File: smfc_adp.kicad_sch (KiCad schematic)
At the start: 29 parts, among them J1 Conn_01x03_Pin, J11 Conn_01x02_Socket, J2 Conn_01x03_Pin, J25 Conn_01x02_Socket, J26 Conn_01x02_Socket, J4 Conn_01x04_Socket, U1 ADP5091

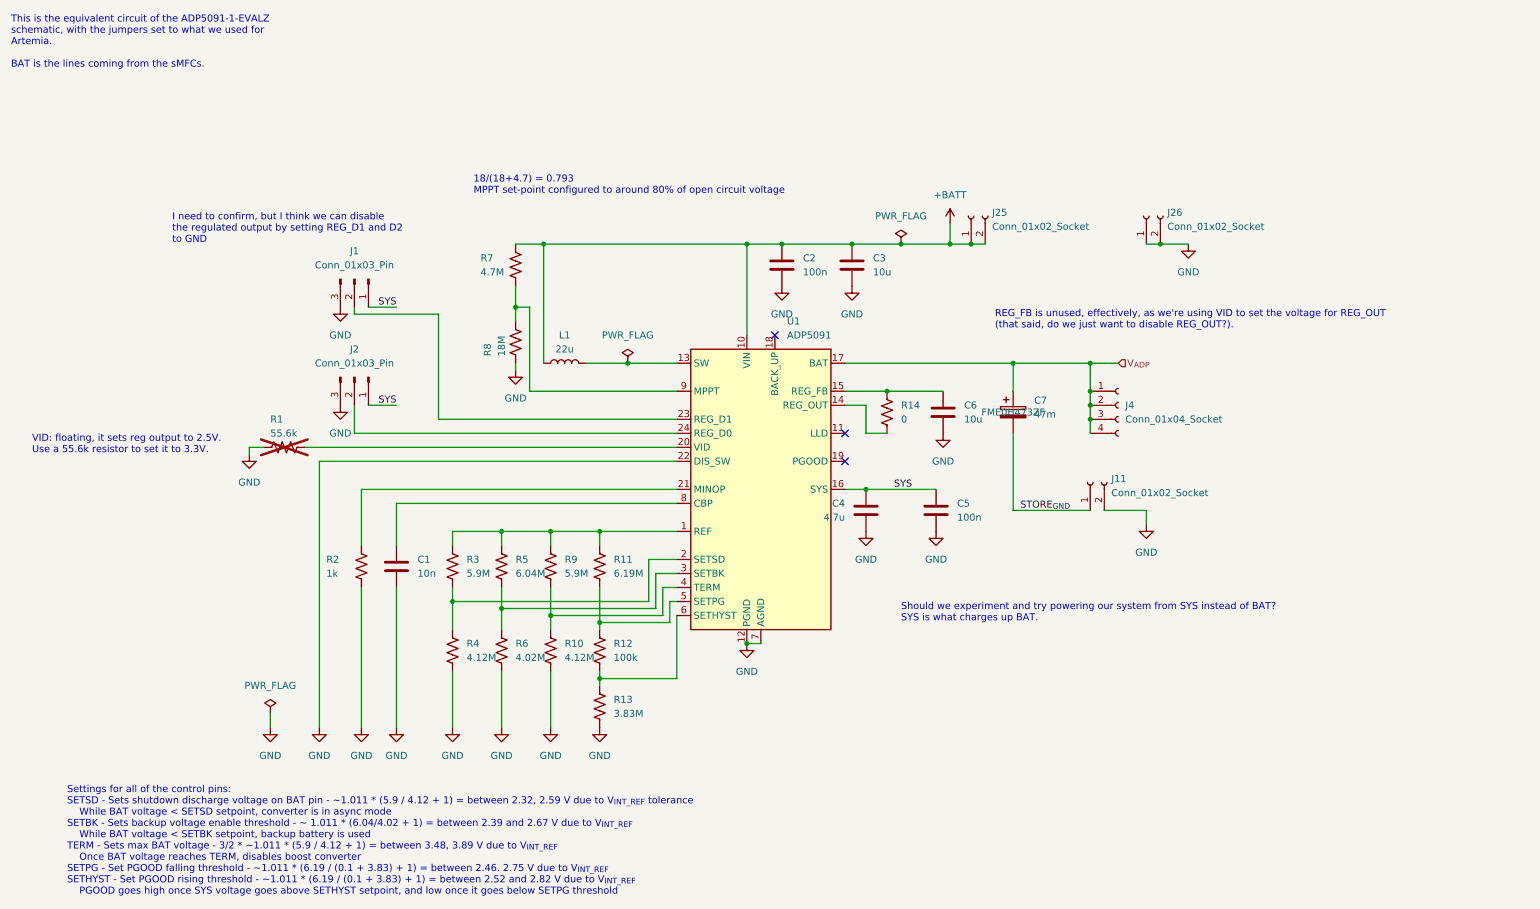
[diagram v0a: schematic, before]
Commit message: Add more informative text, crystal to SMD, headers
 - Added a lot more to the silkscreen to segment parts of the board
 - Changed the 32kHz crystals to an SMD part
 - Added some headers for ADP5091 function
 - Some BOM consolidation, mostly of resistors and capacitors
 - Marked one capacitor as C0G rating
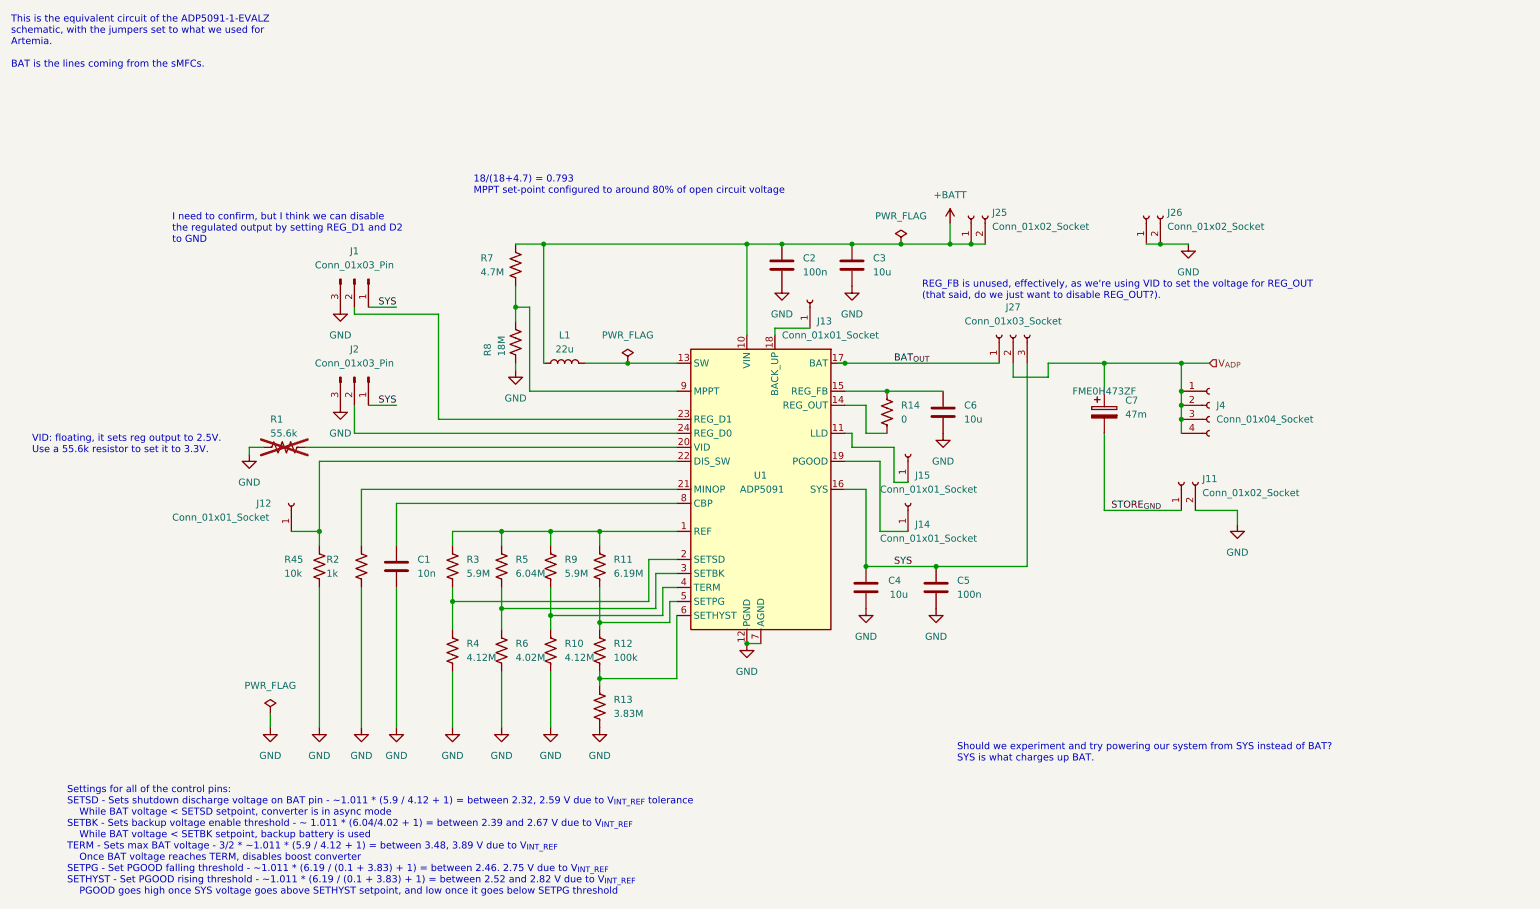
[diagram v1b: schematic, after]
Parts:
- added J12, J13, J14, J15: Conn_01x01_Socket, Connector_PinHeader_2.54mm:PinHeader_1x01_P2.54mm_Vertical, symbol Connector:Conn_01x01_Socket
- added J27: Conn_01x03_Socket, Connector_PinHeader_2.54mm:PinHeader_1x03_P2.54mm_Vertical, symbol Connector:Conn_01x03_Socket
- added R45: 10k, Resistor_SMD:R_0603_1608Metric_Pad0.98x0.95mm_HandSolder, symbol Device:R_US
- C1: Digikey Product Number (none) -> 490-GRT1885C1E103JA02JTR-ND; Manufacturer Product Number (none) -> GRT1885C1E103JA02J
- C4: value 4.7u -> 10u
- C7: Digikey Product Number (none) -> 399-13100-ND
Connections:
- net GND: now also R45.1; no longer U1.22 (DIS_SW)
- net SYS: now also J27.3 (Pin_3)
- net V_{ADP}: now also J27.2 (Pin_2); no longer U1.17 (BAT)
- net at U1.11 (LLD): now also J15.1 (Pin_1)
- net at U1.18 (BACK_UP): now also J13.1 (Pin_1)
- net at U1.19 (PGOOD): now also J14.1 (Pin_1)
- new net: J12.1 (Pin_1), R45.2, U1.22 (DIS_SW)
- new net BAT_{OUT}: J27.1 (Pin_1), U1.17 (BAT)
- no-connect marks 3 -> 0
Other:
- moved on the sheet: C4, C5, C7, J11, J4

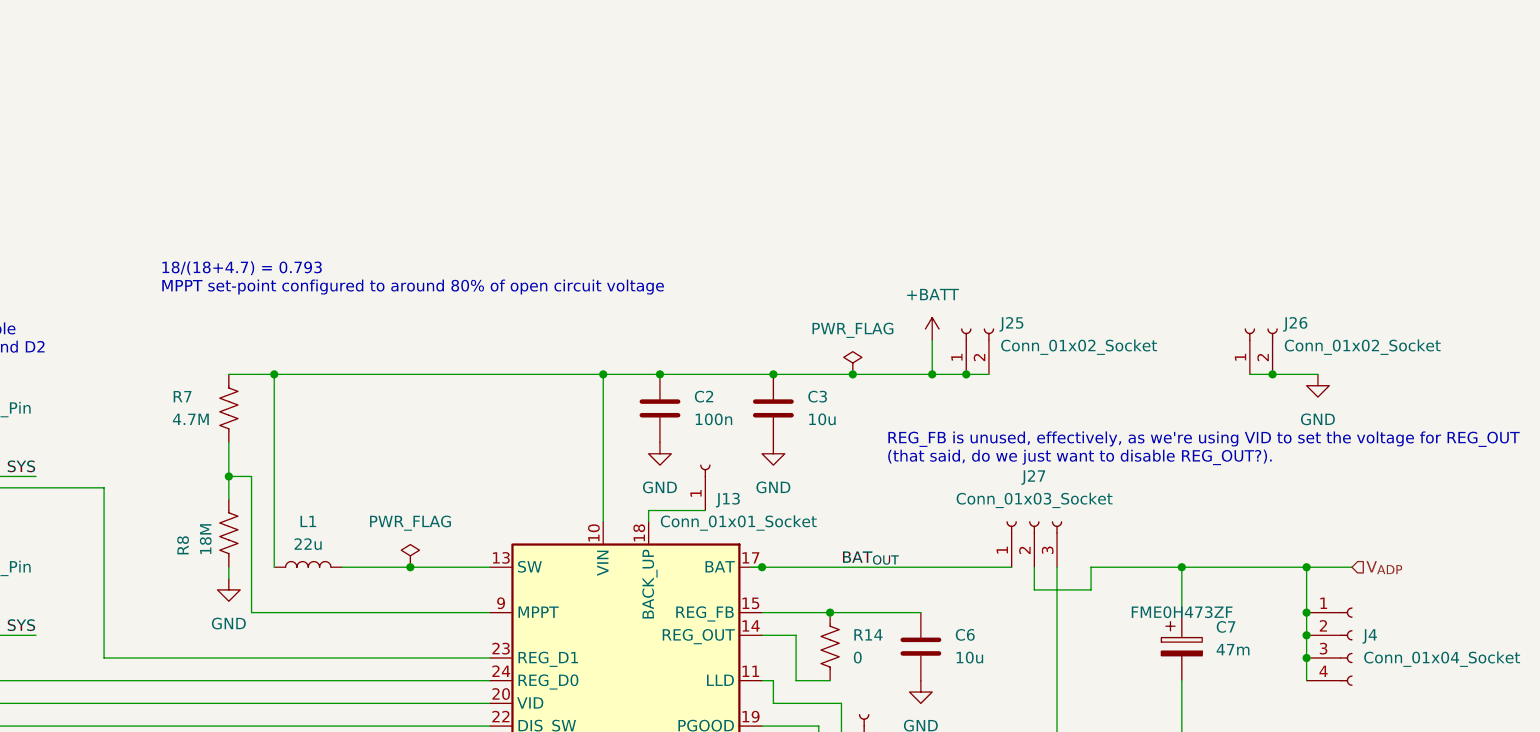
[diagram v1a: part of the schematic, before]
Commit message: Fix ERC, add MPN and datasheet information
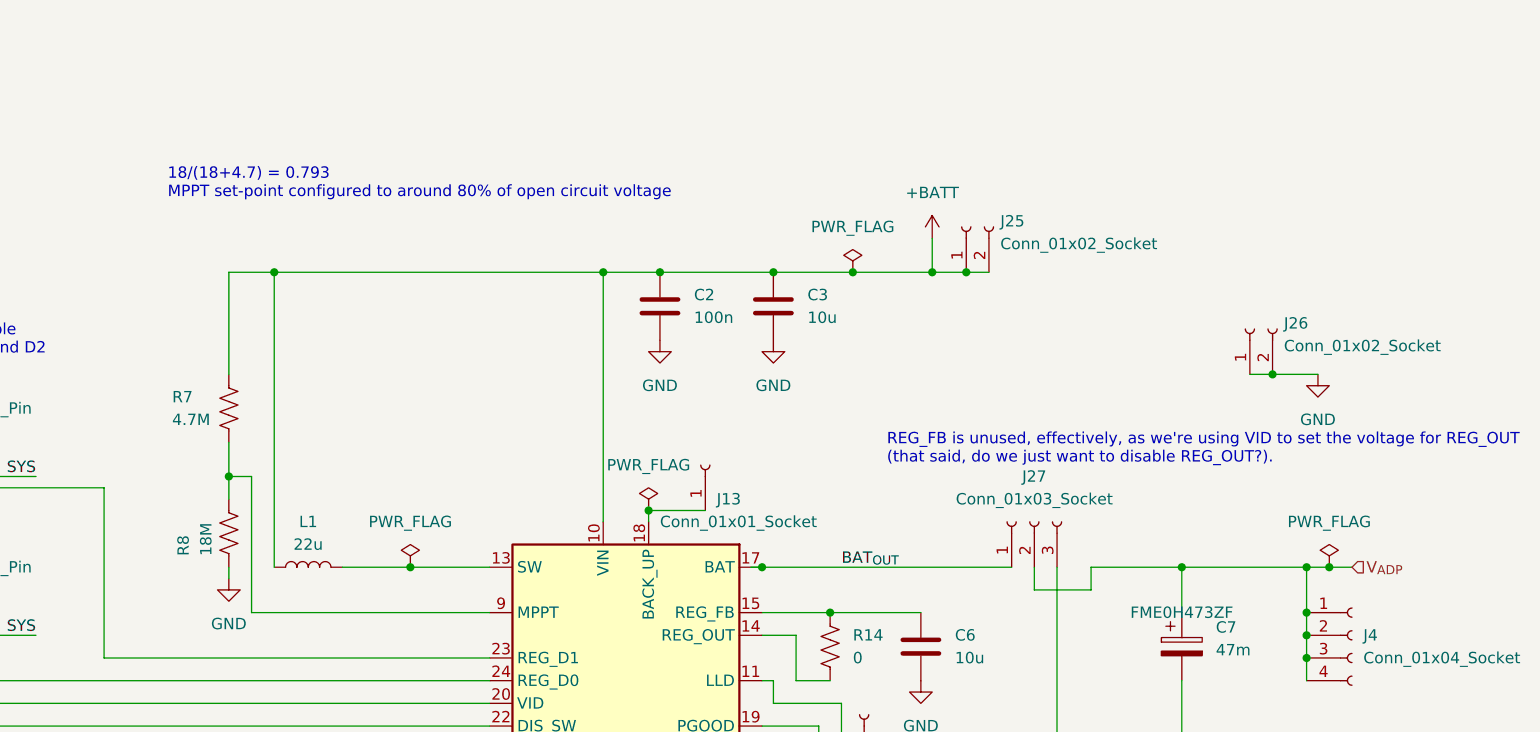
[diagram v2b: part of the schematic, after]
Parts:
- U1: Digikey Product Number (none) -> 505-ADP5091ACPZ-1-R7TR-ND; Manufacturer Product Number (none) -> ADP5091ACPZ-1-R7
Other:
- moved on the sheet: C2, C3, J25

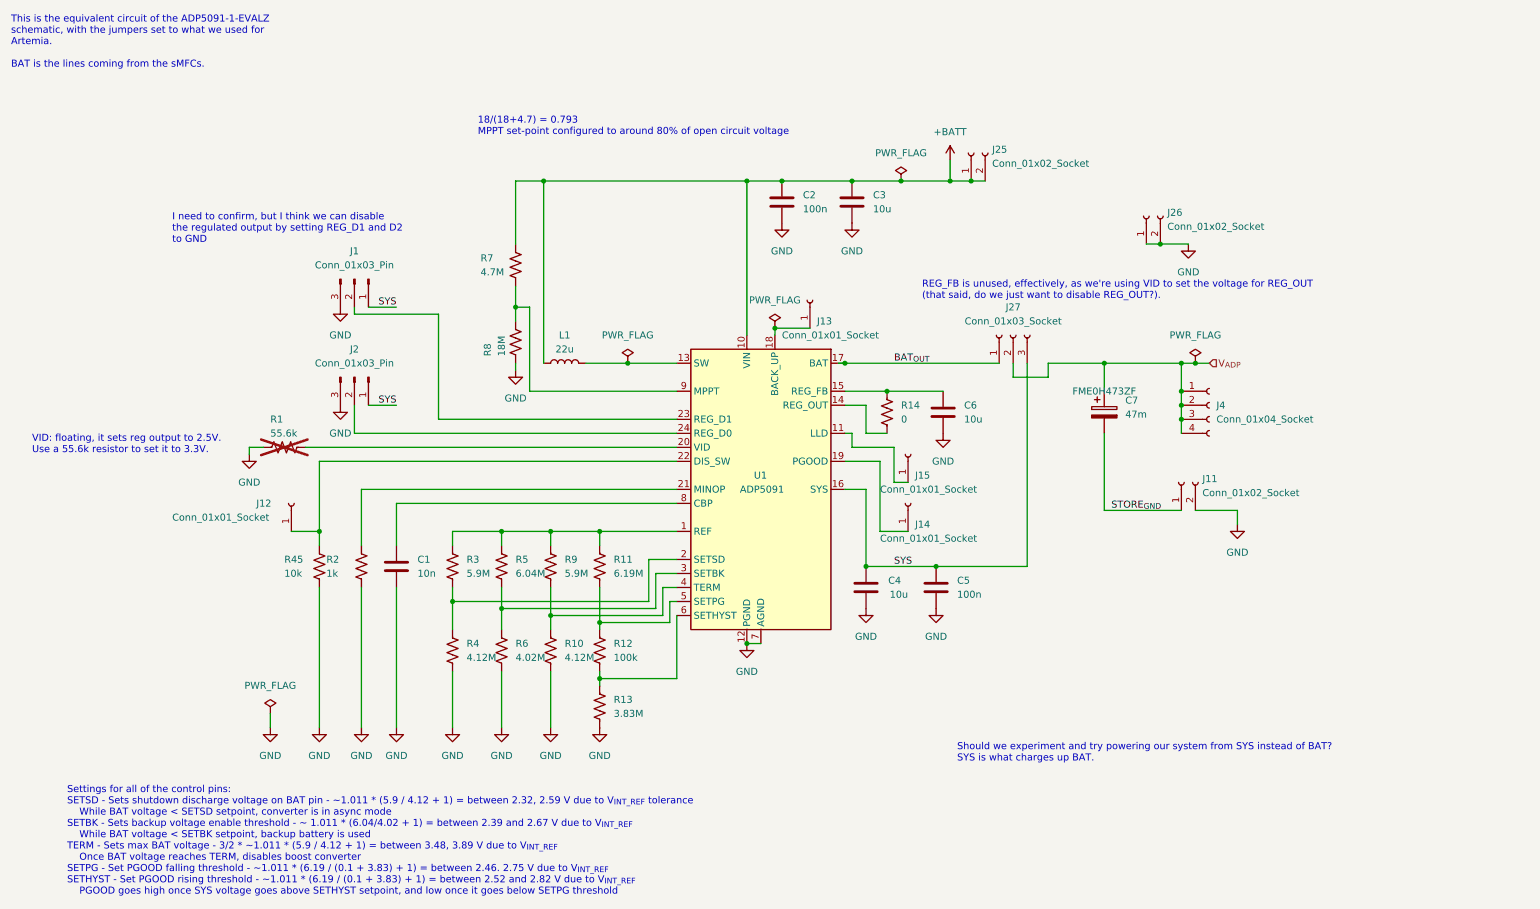
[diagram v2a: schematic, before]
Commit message: Update datasheet and MPN for C and R
 - Update pin headers from sockets to pins
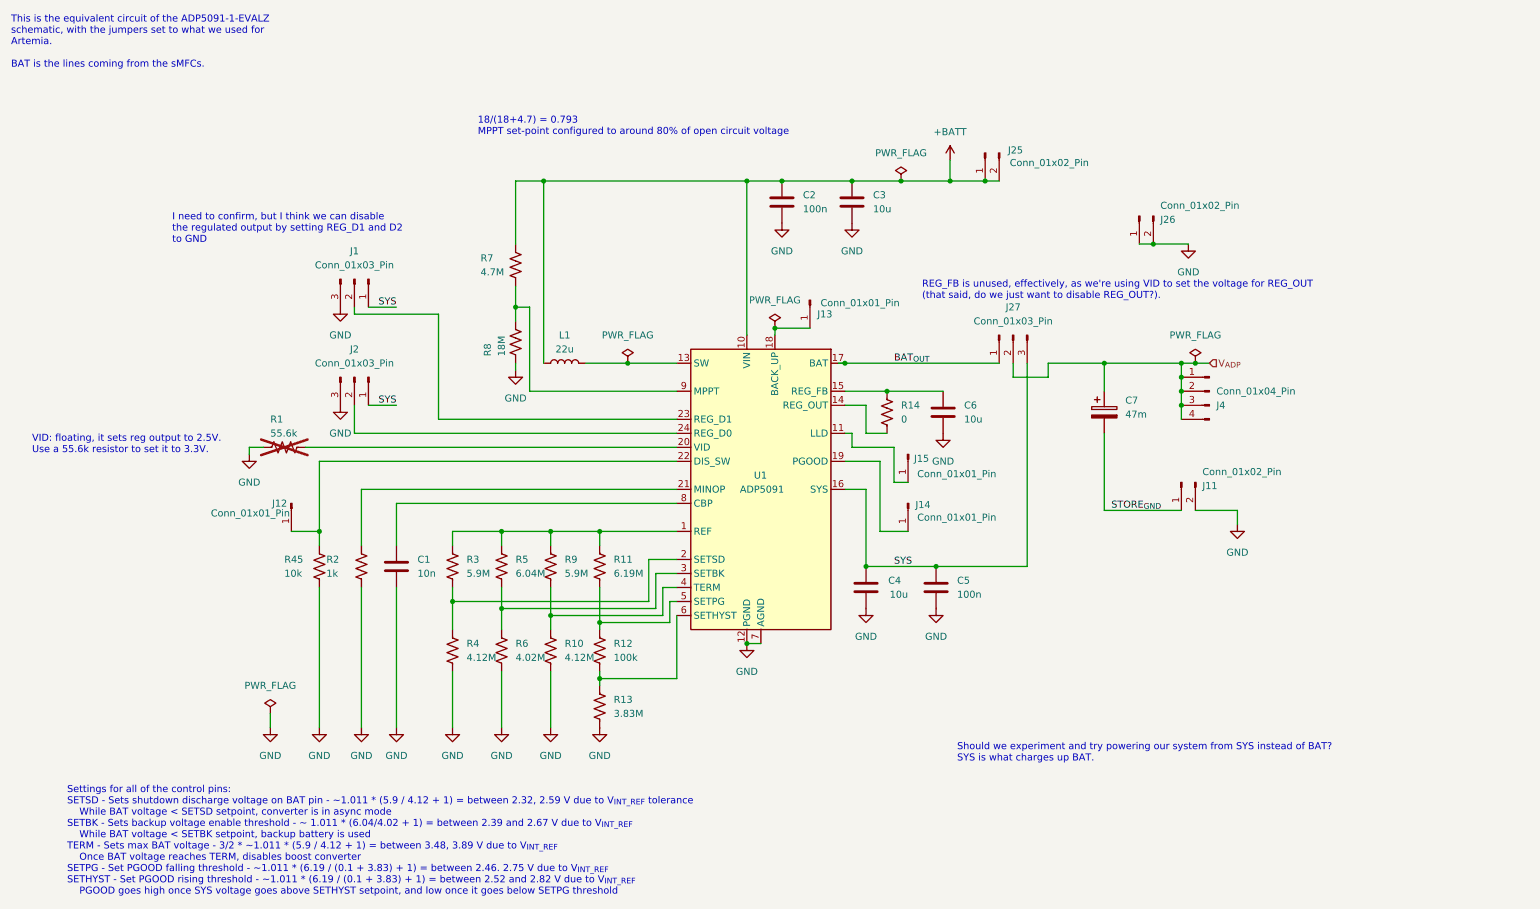
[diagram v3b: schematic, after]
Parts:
- C2, C5: Digikey Product Number (none) -> 1276-1935-2-ND; Manufacturer Product Number (none) -> CL10B104KB8NNWC
- C3, C4, C6: Digikey Product Number (none) -> 1276-CL10A106KP8NNWCTR-ND; Manufacturer Product Number (none) -> CL10A106KP8NNWC
- J11, J25, J26: value Conn_01x02_Socket -> Conn_01x02_Pin; symbol Connector:Conn_01x02_Socket -> Connector:Conn_01x02_Pin
- J12, J13, J14, J15: value Conn_01x01_Socket -> Conn_01x01_Pin; symbol Connector:Conn_01x01_Socket -> Connector:Conn_01x01_Pin
- J27: value Conn_01x03_Socket -> Conn_01x03_Pin; symbol Connector:Conn_01x03_Socket -> Connector:Conn_01x03_Pin
- J4: value Conn_01x04_Socket -> Conn_01x04_Pin; symbol Connector:Conn_01x04_Socket -> Connector:Conn_01x04_Pin
- R1: Digikey Product Number (none) -> RMCF0603FT56K0TR-ND; Manufacturer Product Number (none) -> RMCF0603FT56K0
- R10, R4: Digikey Product Number (none) -> 13-RC0603FR-074M12LTR-ND; Manufacturer Product Number (none) -> RC0603FR-074M12L
- R11: Digikey Product Number (none) -> RMCF0603FT6M19TR-ND; Manufacturer Product Number (none) -> RMCF0603FT6M19
- R12: Digikey Product Number (none) -> 1292-WR06X1003FTLTR-ND; Manufacturer Product Number (none) -> WR06X1003FTL
- R13: Digikey Product Number (none) -> RMCF0603FT3M83TR-ND; Manufacturer Product Number (none) -> RMCF0603FT3M83
- R14: Digikey Product Number (none) -> RMCF0603ZT0R00TR-ND; Manufacturer Product Number (none) -> RMCF0603ZT0R00
- R2: Digikey Product Number (none) -> RMCF0603FT1K00TR-ND; Manufacturer Product Number (none) -> RMCF0603FT1K00
- R3, R9: Digikey Product Number (none) -> RMCF0603FT5M90TR-ND; Manufacturer Product Number (none) -> RMCF0603FT5M90
- R45: Digikey Product Number (none) -> RMCF0603FT10K0TR-ND; Manufacturer Product Number (none) -> RMCF0603FT10K0
- R5: Digikey Product Number (none) -> RMCF0603FT6M04TR-ND; Manufacturer Product Number (none) -> RMCF0603FT6M04
- R6: Digikey Product Number (none) -> YAG5698TR-ND; Manufacturer Product Number (none) -> RC0603FR-074M02L
- R7: Digikey Product Number (none) -> 13-RC0603FR-134M7LTR-ND; Manufacturer Product Number (none) -> RC0603FR-134M7L
- R8: Digikey Product Number (none) -> 2019-RK73B1JTTD186JTR-ND; Manufacturer Product Number (none) -> RK73B1JTTD186J

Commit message: Fix BSS123 pins, remove R18 R19 pulldowns
 - BSS123 pinout were completely wrong due to using the wrong symbol in
   the schematic. Made a new symbol with the right pinout. Fixes #7.
 - R18 and R19 were forming a voltage divider as V_GOOD and EN_PULSE
   are open-drain lines. Remove the pull-downs, and pray that circuit
   initialization is sane. Fixes #6.
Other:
- title: Artemia: Energy Harvesting Subsystem -> Artemia: Power Management Subsystem
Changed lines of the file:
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@@
 	(paper "USLetter")
 	(title_block
-		(title "Artemia: Energy Harvesting Subsystem")
-		(date "2024-04-09")
-		(rev "A")
+		(title "Artemia: Power Management Subsystem")
+		(date "2024-11-21")
+		(rev "B*")
 		(company "UC San Diego")
 		(comment 1 "Author: ${AUTHOR}")
